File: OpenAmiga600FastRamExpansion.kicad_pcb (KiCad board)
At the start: 2 copper layers, 72.3 x 72.5 mm, 27 parts, among them J1 MC68000_PLCC68, P1 JTAG_CONNECTOR, P98 SCREW_HOLE, P99 OSHW_LOGO, U1 74LS157, U2 74LS157, U3 HYB5118160BSJ, U4 HYB5118160BSJ, U5 ATF1502AS-10JU44

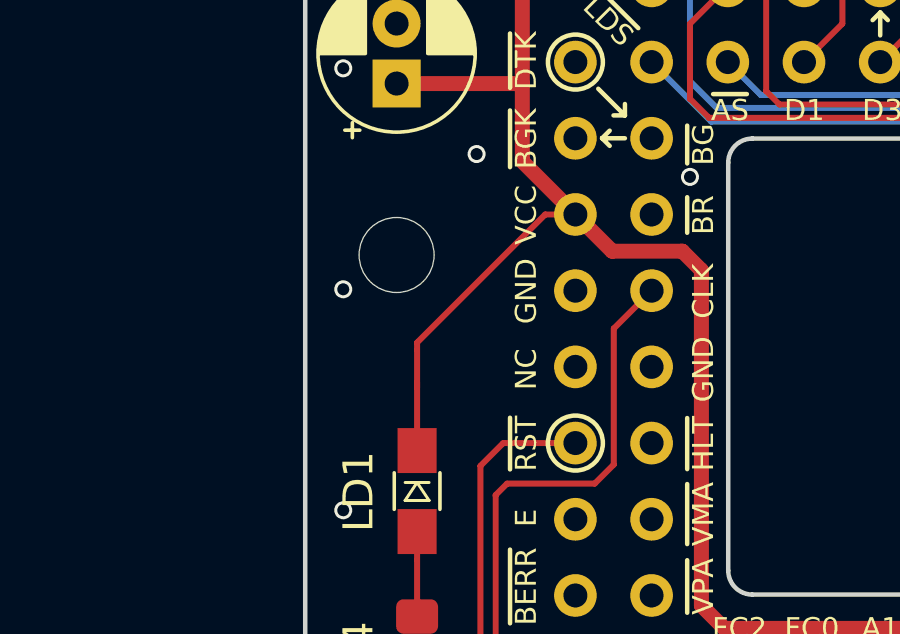
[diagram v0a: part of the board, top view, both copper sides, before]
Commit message: Connect screw hole to ground plate
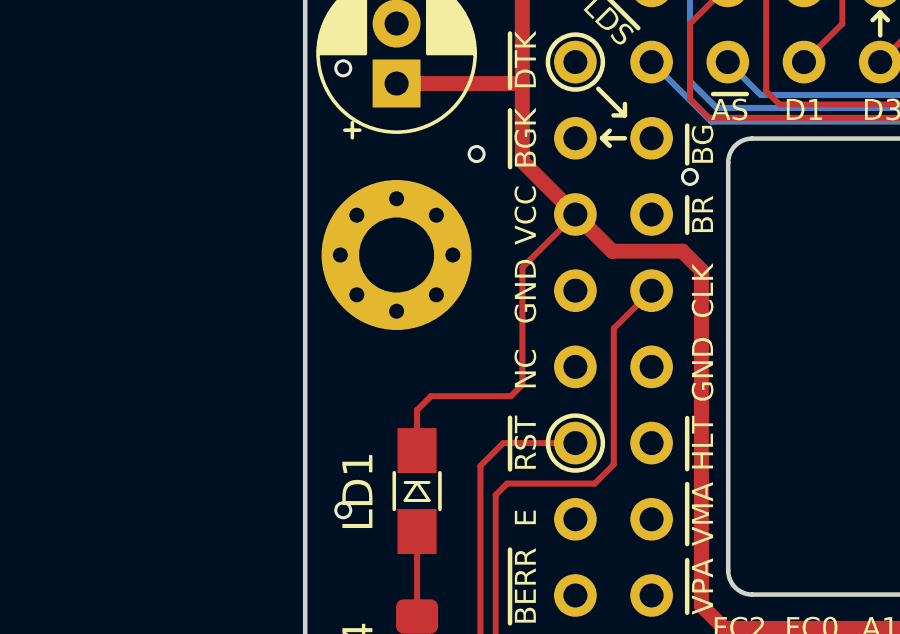
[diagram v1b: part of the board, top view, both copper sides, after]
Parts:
- P98: footprint MountingHole:MountingHole_2.5mm -> MountingHole:MountingHole_2.5mm_Pad_Via
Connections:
- P98 pad 1: (no net) -> GND
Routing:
- net VCC: track 319.6 -> 320.4 mm
- net GND: vias 168 -> 167
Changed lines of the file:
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@@
     (thickness 1.6)
     (drawings 102)
-    (tracks 1221)
+    (tracks 1220)
     (zones 0)
     (modules 27)
@@
     )
   )
-  (module MountingHole:MountingHole_2.5mm (layer F.Cu)
-    (at 114.046 101.981)
-    (descr "Mounting Hole 2.5mm, no annular")
-    (tags "mounting hole 2.5mm no annular")
-    (attr virtual)
-    (fp_text reference P98 (at 0 -3.5) (layer F.SilkS) hide
-      (effects (font (size 1 1) (thickness 0.15)))
-    )
-    (fp_text value SCREW_HOLE (at 0 3.5) (layer F.Fab)
-      (effects (font (size 1 1) (thickness 0.15)))
-    )
-    (fp_circle (center 0 0) (end 2.75 0) (layer F.CrtYd) (width 0.05))
-    (fp_circle (center 0 0) (end 2.5 0) (layer Cmts.User) (width 0.15))
-    (fp_text user %R (at 0.3 0) (layer F.Fab)
-      (effects (font (size 1 1) (thickness 0.15)))
-    )
-    (pad 1 np_thru_hole circle (at 0 0) (size 2.5 2.5) (drill 2.5) (layers *.Cu *.Mask))
-  )
   (module Package_SO:SOIC-16_3.9x9.9mm_P1.27mm (layer F.Cu)
     (at 172.7 77.06 90)
@@
       (rotate (xyz 0 0 0))
     )
+  )
+  (module MountingHole:MountingHole_2.5mm_Pad_Via (layer F.Cu)
+    (at 114.046 101.981)
+    (descr "Mounting Hole 2.5mm")
+    (tags "mounting hole 2.5mm")
+    (zone_connect 2)
+    (attr virtual)
+    (fp_text reference P98 (at 0 -3.5) (layer F.SilkS) hide
+      (effects (font (size 1 1) (thickness 0.15)))
+    )
+    (fp_text value SCREW_HOLE (at 0 3.5) (layer F.Fab)
+      (effects (font (size 1 1) (thickness 0.15)))
+    )
+    (fp_text user %R (at 0.3 0) (layer F.Fab)
+      (effects (font (size 1 1) (thickness 0.15)))
+    )
+    (fp_circle (center 0 0) (end 2.5 0) (layer Cmts.User) (width 0.15))
+    (fp_circle (center 0 0) (end 2.75 0) (layer F.CrtYd) (width 0.05))
+    (pad 1 thru_hole circle (at 0 0) (size 5 5) (drill 2.5) (layers *.Cu *.Mask)
+      (net 18 GND) (zone_connect 2))
+    (pad 1 thru_hole circle (at 1.875 0) (size 0.8 0.8) (drill 0.5) (layers *.Cu *.Mask)
+      (net 18 GND) (zone_connect 2))
+    (pad 1 thru_hole circle (at 1.325825 1.325825) (size 0.8 0.8) (drill 0.5) (layers *.Cu *.Mask)
+      (net 18 GND) (zone_connect 2))
+    (pad 1 thru_hole circle (at 0 1.875) (size 0.8 0.8) (drill 0.5) (layers *.Cu *.Mask)
+      (net 18 GND) (zone_connect 2))
+    (pad 1 thru_hole circle (at -1.325825 1.325825) (size 0.8 0.8) (drill 0.5) (layers *.Cu *.Mask)
+      (net 18 GND) (zone_connect 2))
+    (pad 1 thru_hole circle (at -1.875 0) (size 0.8 0.8) (drill 0.5) (layers *.Cu *.Mask)
+      (net 18 GND) (zone_connect 2))
+    (pad 1 thru_hole circle (at -1.325825 -1.325825) (size 0.8 0.8) (drill 0.5) (layers *.Cu *.Mask)
+      (net 18 GND) (zone_connect 2))
+    (pad 1 thru_hole circle (at 0 -1.875) (size 0.8 0.8) (drill 0.5) (layers *.Cu *.Mask)
+      (net 18 GND) (zone_connect 2))
+    (pad 1 thru_hole circle (at 1.325825 -1.325825) (size 0.8 0.8) (drill 0.5) (layers *.Cu *.Mask)
+      (net 18 GND) (zone_connect 2))
   )
   (dimension 33.5 (width 0.3) (layer F.CrtYd)
@@
   (via (at 112.268 117.856) (size 0.6) (drill 0.4) (layers F.Cu B.Cu) (net 18))
   (via (at 112.268 110.49) (size 0.6) (drill 0.4) (layers F.Cu B.Cu) (net 18))
-  (via (at 112.268 103.124) (size 0.6) (drill 0.4) (layers F.Cu B.Cu) (net 18))
   (via (at 112.268 95.758) (size 0.6) (drill 0.4) (layers F.Cu B.Cu) (net 18))
   (via (at 112.268 88.392) (size 0.6) (drill 0.4) (layers F.Cu B.Cu) (net 18))
@@
   (segment (start 153.283 113.293) (end 153.306 113.27) (width 0.5) (layer B.Cu) (net 19))
   (segment (start 181.283 110.69) (end 179.89 110.69) (width 0.2) (layer F.Cu) (net 19))
-  (segment (start 120.006 100.63) (end 119.000212 100.63) (width 0.2) (layer F.Cu) (net 19))
-  (segment (start 119.000212 100.63) (end 114.728843 104.901369) (width 0.2) (layer F.Cu) (net 19))
-  (segment (start 114.728843 104.901369) (end 114.728843 105.154432) (width 0.2) (layer F.Cu) (net 19))
   (segment (start 118.237 98.861) (end 120.006 100.63) (width 0.5) (layer F.Cu) (net 19))
   (segment (start 119.253 89.7255) (end 118.237 90.7415) (width 0.5) (layer F.Cu) (net 19))
@@
   (segment (start 173.609 108.195) (end 174.743 108.195) (width 0.2) (layer B.Cu) (net 19))
   (segment (start 179.714 103.378) (end 179.714 105.537) (width 0.2) (layer F.Cu) (net 19))
-  (segment (start 114.728843 105.154432) (end 114.728843 106.2355) (width 0.2) (layer F.Cu) (net 19))
-  (segment (start 114.728843 106.2355) (end 114.728843 108.499932) (width 0.2) (layer F.Cu) (net 19))
-  (segment (start 114.728843 106.2355) (end 114.728843 106.404432) (width 0.2) (layer F.Cu) (net 19))
   (segment (start 180.848 120.904) (end 179.714 120.904) (width 0.2) (layer F.Cu) (net 19))
   (segment (start 181.356 106.045) (end 181.356 120.396) (width 0.2) (layer F.Cu) (net 19))
@@
   (segment (start 152.427 78.459) (end 152.427 84.298) (width 0.5) (layer F.Cu) (net 19))
   (segment (start 153.171 77.715) (end 152.427 78.459) (width 0.5) (layer F.Cu) (net 19))
+  (segment (start 117.858 106.688) (end 118.239 106.307) (width 0.2) (layer F.Cu) (net 19))
+  (segment (start 115.191 106.688) (end 117.858 106.688) (width 0.2) (layer F.Cu) (net 19))
+  (segment (start 118.239 102.397) (end 120.006 100.63) (width 0.2) (layer F.Cu) (net 19))
+  (segment (start 118.239 106.307) (end 118.239 102.397) (width 0.2) (layer F.Cu) (net 19))
+  (segment (start 114.728843 107.150157) (end 115.191 106.688) (width 0.2) (layer F.Cu) (net 19))
+  (segment (start 114.728843 108.499932) (end 114.728843 107.150157) (width 0.2) (layer F.Cu) (net 19))
   (segment (start 163.8108 101.854) (end 165.862 101.854) (width 0.2) (layer F.Cu) (net 20))
   (segment (start 163.466 102.1988) (end 163.8108 101.854) (width 0.2) (layer F.Cu) (net 20))

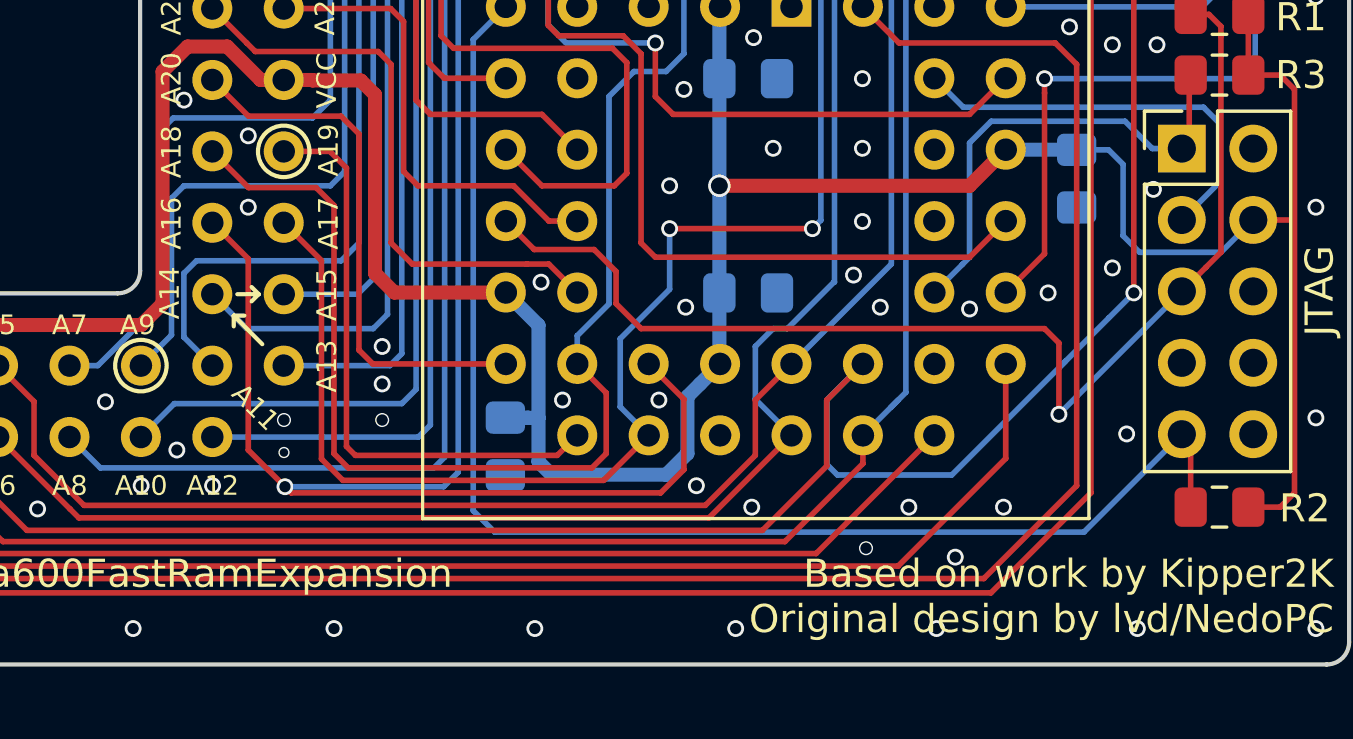
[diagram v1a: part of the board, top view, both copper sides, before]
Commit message: Add version number and update renders
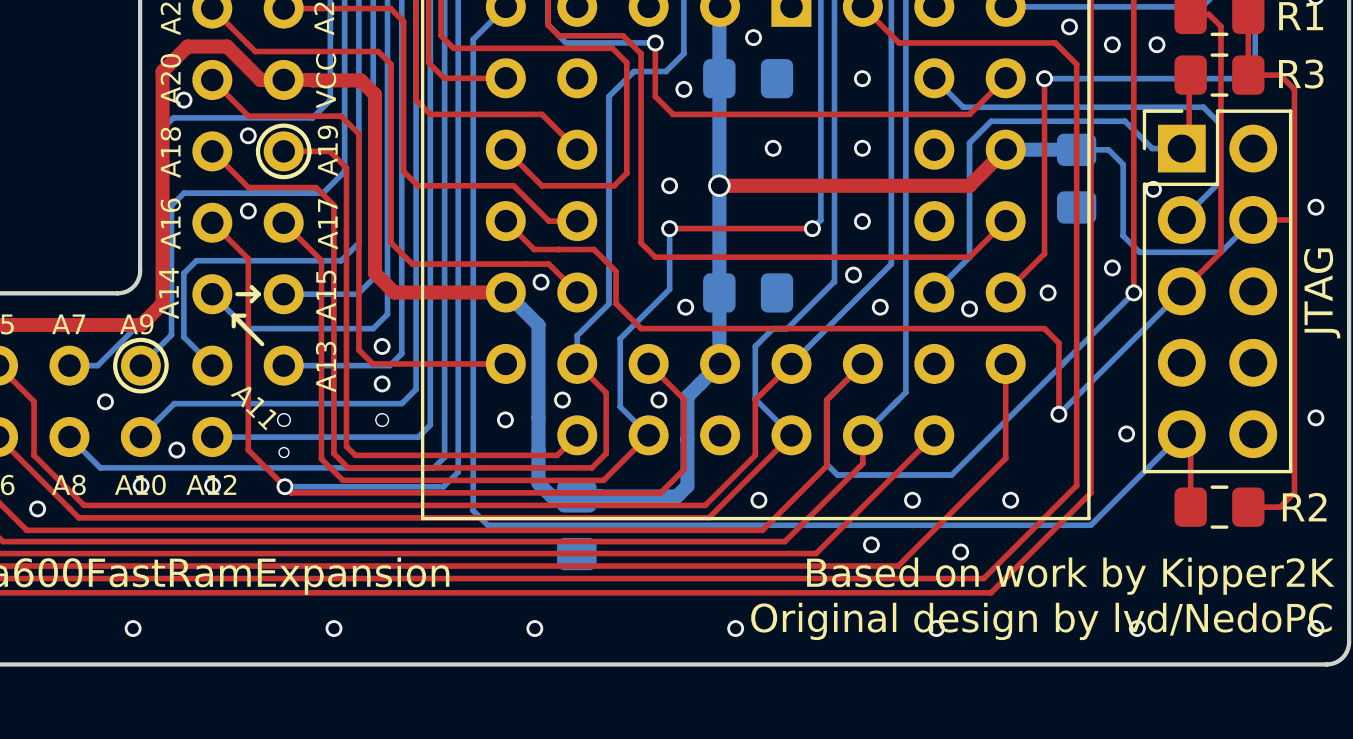
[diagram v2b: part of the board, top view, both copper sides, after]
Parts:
- moved C10 3.78 mm to (155.8, 121.5)
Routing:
- net VCC: track 320.4 -> 321.0 mm
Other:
- board text added: "V1"
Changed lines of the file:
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@@
   (general
     (thickness 1.6)
-    (drawings 102)
-    (tracks 1220)
+    (drawings 103)
+    (tracks 1225)
     (zones 0)
     (modules 27)
@@
   )
   (module Capacitor_SMD:C_0805_2012Metric_Pad1.15x1.40mm_HandSolder (layer B.Cu)
-    (at 153.289 118.745 270)
+    (at 155.831 121.547 270)
     (descr "Capacitor SMD 0805 (2012 Metric), square (rectangular) end terminal, IPC_7351 nominal with elongated pad for handsoldering. (Body size source: https://docs.google.com/spreadsheets/d/1BsfQQcO9C6DZCsRaXUlFlo91Tg2WpOkGARC1WS5S8t0/edit?usp=sharing), generated with kicad-footprint-generator")
     (tags "capacitor handsolder")
@@
       (net 18 GND) (zone_connect 2))
   )
+  (gr_text V1 (at 113.3495 124.214) (layer B.SilkS)
+    (effects (font (size 1 1) (thickness 0.2)) (justify mirror))
+  )
   (dimension 33.5 (width 0.3) (layer F.CrtYd)
     (gr_text "33,500 mm" (at 115.9 70.75 90) (layer F.CrtYd)
@@
   (via (at 155.321 117.094) (size 0.6) (drill 0.4) (layers F.Cu B.Cu) (net 18))
   (via (at 158.75 117.094) (size 0.6) (drill 0.4) (layers F.Cu B.Cu) (net 18))
-  (via (at 160.0835 120.142) (size 0.6) (drill 0.4) (layers F.Cu B.Cu) (net 18))
-  (via (at 162.052 120.904) (size 0.6) (drill 0.4) (layers F.Cu B.Cu) (net 18))
-  (via (at 166.116 122.3645) (size 0.5) (drill 0.4) (layers F.Cu B.Cu) (net 18))
-  (via (at 169.291 122.682) (size 0.6) (drill 0.4) (layers F.Cu B.Cu) (net 18))
-  (via (at 167.64 120.904) (size 0.6) (drill 0.4) (layers F.Cu B.Cu) (net 18))
-  (via (at 171.0055 120.904) (size 0.6) (drill 0.4) (layers F.Cu B.Cu) (net 18))
+  (via (at 162.308 120.658) (size 0.6) (drill 0.4) (layers F.Cu B.Cu) (net 18))
+  (via (at 166.3085 122.2455) (size 0.6) (drill 0.4) (layers F.Cu B.Cu) (net 18))
+  (via (at 169.4835 122.4995) (size 0.6) (drill 0.4) (layers F.Cu B.Cu) (net 18))
+  (via (at 167.769 120.658) (size 0.6) (drill 0.4) (layers F.Cu B.Cu) (net 18))
+  (via (at 171.2615 120.658) (size 0.6) (drill 0.4) (layers F.Cu B.Cu) (net 18))
   (via (at 175.387 118.3005) (size 0.6) (drill 0.4) (layers F.Cu B.Cu) (net 18))
   (via (at 159.7025 113.792) (size 0.6) (drill 0.4) (layers F.Cu B.Cu) (net 18))
@@
   (via (at 141.859 106.426) (size 0.6) (drill 0.4) (layers F.Cu B.Cu) (net 18))
   (via (at 144.145 107.696) (size 0.6) (drill 0.4) (layers F.Cu B.Cu) (net 18))
-  (via (at 144.145 110.236) (size 0.6) (drill 0.4) (layers F.Cu B.Cu) (net 18))
   (via (at 147.32 91.2495) (size 0.6) (drill 0.4) (layers F.Cu B.Cu) (net 18))
   (via (at 147.4216 93.6244) (size 0.6) (drill 0.4) (layers F.Cu B.Cu) (net 18))
@@
   (via (at 142.0114 82.042) (size 0.6) (drill 0.4) (layers F.Cu B.Cu) (net 18))
   (via (at 143.51 78.867) (size 0.6) (drill 0.4) (layers F.Cu B.Cu) (net 18))
+  (via (at 153.291 117.8005) (size 0.6) (drill 0.4) (layers F.Cu B.Cu) (net 18))
+  (via (at 144.147 110.371) (size 0.6) (drill 0.4) (layers F.Cu B.Cu) (net 18))
   (segment (start 165.6 76.075) (end 167.925 76.075) (width 0.5) (layer F.Cu) (net 19))
   (segment (start 168.255 75.745) (end 168.255 74.36) (width 0.5) (layer F.Cu) (net 19))
@@
   (segment (start 159.764799 116.971201) (end 160.214801 116.521199) (width 0.5) (layer B.Cu) (net 19))
   (segment (start 153.306 113.27) (end 154.467201 114.431201) (width 0.5) (layer B.Cu) (net 19))
-  (segment (start 159.764799 119.000201) (end 159.764799 116.971201) (width 0.5) (layer B.Cu) (net 19))
-  (segment (start 154.467201 119.288201) (end 154.931 119.752) (width 0.5) (layer B.Cu) (net 19))
-  (segment (start 154.931 119.752) (end 159.013 119.752) (width 0.5) (layer B.Cu) (net 19))
-  (segment (start 159.013 119.752) (end 159.764799 119.000201) (width 0.5) (layer B.Cu) (net 19))
-  (segment (start 154.098 117.729) (end 154.467201 117.729) (width 0.5) (layer B.Cu) (net 19))
   (segment (start 154.467201 114.431201) (end 154.467201 117.729) (width 0.5) (layer B.Cu) (net 19))
-  (segment (start 154.089 117.72) (end 154.098 117.729) (width 0.5) (layer B.Cu) (net 19))
-  (segment (start 153.289 117.72) (end 154.089 117.72) (width 0.5) (layer B.Cu) (net 19))
-  (segment (start 154.467201 117.729) (end 154.467201 119.288201) (width 0.5) (layer B.Cu) (net 19))
   (segment (start 165.608 88.011) (end 165.608 89.145) (width 0.5) (layer F.Cu) (net 19))
   (segment (start 164.973 87.376) (end 165.608 88.011) (width 0.5) (layer F.Cu) (net 19))
@@
   (segment (start 114.728843 107.150157) (end 115.191 106.688) (width 0.2) (layer F.Cu) (net 19))
   (segment (start 114.728843 108.499932) (end 114.728843 107.150157) (width 0.2) (layer F.Cu) (net 19))
+  (segment (start 155.831 120.522) (end 154.933 120.522) (width 0.5) (layer B.Cu) (net 19))
+  (segment (start 154.467201 120.056201) (end 154.467201 118.88) (width 0.5) (layer B.Cu) (net 19))
+  (segment (start 154.933 120.522) (end 154.467201 120.056201) (width 0.5) (layer B.Cu) (net 19))
+  (segment (start 154.467201 117.729) (end 154.467201 118.88) (width 0.5) (layer B.Cu) (net 19))
+  (segment (start 156.631 120.522) (end 156.64 120.531) (width 0.5) (layer B.Cu) (net 19))
+  (segment (start 155.831 120.522) (end 156.631 120.522) (width 0.5) (layer B.Cu) (net 19))
+  (segment (start 156.631 120.522) (end 159.396 120.522) (width 0.5) (layer B.Cu) (net 19))
+  (segment (start 159.764799 120.153201) (end 159.764799 118.499) (width 0.5) (layer B.Cu) (net 19))
+  (segment (start 159.396 120.522) (end 159.764799 120.153201) (width 0.5) (layer B.Cu) (net 19))
+  (segment (start 159.764799 118.499) (end 159.764799 116.971201) (width 0.5) (layer B.Cu) (net 19))
   (segment (start 163.8108 101.854) (end 165.862 101.854) (width 0.2) (layer F.Cu) (net 20))
   (segment (start 163.466 102.1988) (end 163.8108 101.854) (width 0.2) (layer F.Cu) (net 20))
@@
   (segment (start 173.99 78.359) (end 173.99 81.026) (width 0.2) (layer F.Cu) (net 25))
   (via (at 173.99 81.026) (size 0.6) (drill 0.4) (layers F.Cu B.Cu) (net 25))
-  (segment (start 141.4145 114.7815) (end 140.326 115.87) (width 0.2) (layer B.Cu) (net 25))
-  (segment (start 141.4145 109.9185) (end 141.4145 114.7815) (width 0.2) (layer B.Cu) (net 25))
-  (segment (start 141.859 109.474) (end 141.4145 109.9185) (width 0.2) (layer B.Cu) (net 25))
-  (segment (start 147.066 109.474) (end 141.859 109.474) (width 0.2) (layer B.Cu) (net 25))
-  (segment (start 147.574 108.966) (end 147.066 109.474) (width 0.2) (layer B.Cu) (net 25))
+  (segment (start 141.859 109.736) (end 141.4145 110.1805) (width 0.2) (layer B.Cu) (net 25))
+  (segment (start 146.804 109.736) (end 141.859 109.736) (width 0.2) (layer B.Cu) (net 25))
   (segment (start 173.99 81.026) (end 170.561 81.026) (width 0.2) (layer B.Cu) (net 25))
-  (segment (start 169.926 81.661) (end 161.163 81.661) (width 0.2) (layer B.Cu) (net 25))
   (segment (start 170.561 81.026) (end 169.926 81.661) (width 0.2) (layer B.Cu) (net 25))
   (segment (start 161.163 81.661) (end 147.574 95.25) (width 0.2) (layer B.Cu) (net 25))
+  (segment (start 147.574 108.966) (end 146.804 109.736) (width 0.2) (layer B.Cu) (net 25))
+  (segment (start 141.4145 114.7815) (end 140.326 115.87) (width 0.2) (layer B.Cu) (net 25))
+  (segment (start 141.4145 110.1805) (end 141.4145 114.7815) (width 0.2) (layer B.Cu) (net 25))
+  (segment (start 169.926 81.661) (end 161.163 81.661) (width 0.2) (layer B.Cu) (net 25))
   (segment (start 147.574 95.25) (end 147.574 108.966) (width 0.2) (layer B.Cu) (net 25))
   (segment (start 172.065 76.18) (end 172.72 76.835) (width 0.2) (layer F.Cu) (net 26))
@@
   (segment (start 172.978 117.602) (end 172.978 115.066) (width 0.2) (layer F.Cu) (net 48))
   (segment (start 172.978 115.066) (end 172.466 114.554) (width 0.2) (layer F.Cu) (net 48))
-  (segment (start 156.445201 111.741201) (end 154.317201 111.741201) (width 0.2) (layer F.Cu) (net 48))
   (segment (start 154.317201 111.741201) (end 153.306 110.73) (width 0.2) (layer F.Cu) (net 48))
-  (segment (start 173.867 121.793) (end 177.35 118.31) (width 0.2) (layer B.Cu) (net 49))
-  (segment (start 152.146 121.031) (end 152.908 121.793) (width 0.2) (layer B.Cu) (net 49))
+  (segment (start 155.196 111.741201) (end 155.169201 111.741201) (width 0.2) (layer F.Cu) (net 48))
+  (segment (start 156.445201 111.741201) (end 155.196 111.741201) (width 0.2) (layer F.Cu) (net 48))
+  (segment (start 155.196 111.741201) (end 154.317201 111.741201) (width 0.2) (layer F.Cu) (net 48))
   (segment (start 153.306 103.11) (end 152.146 104.27) (width 0.2) (layer B.Cu) (net 49))
-  (segment (start 152.908 121.793) (end 173.867 121.793) (width 0.2) (layer B.Cu) (net 49))
   (segment (start 152.146 104.27) (end 152.146 121.031) (width 0.2) (layer B.Cu) (net 49))
   (segment (start 177.664 118.624) (end 177.35 118.31) (width 0.2) (layer F.Cu) (net 49))
   (segment (start 177.664 120.904) (end 177.664 118.624) (width 0.2) (layer F.Cu) (net 49))
+  (segment (start 174.113 121.547) (end 174.246 121.414) (width 0.2) (layer B.Cu) (net 49))
+  (segment (start 152.662 121.547) (end 174.113 121.547) (width 0.2) (layer B.Cu) (net 49))
+  (segment (start 174.246 121.414) (end 177.35 118.31) (width 0.2) (layer B.Cu) (net 49))
+  (segment (start 152.146 121.031) (end 152.662 121.547) (width 0.2) (layer B.Cu) (net 49))
   (segment (start 176.3 108.15) (end 177.35 108.15) (width 0.2) (layer B.Cu) (net 50))
   (segment (start 175.328799 107.178799) (end 170.570201 107.178799) (width 0.2) (layer B.Cu) (net 50))
